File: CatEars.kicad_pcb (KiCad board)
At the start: 2 copper layers, 40.1 x 39 mm, 14 parts

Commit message: Added schematic and copper
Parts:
- removed Cuddle, Hugs, Meow, Nya, Puddle: WS2812B, LED_SMD:LED_WS2812B_PLCC4_5.0x5.0mm_P3.2mm
- removed In, Out: Conn_01x03_Female, Connector_PinSocket_2.54mm:PinSocket_1x03_P2.54mm_Vertical
- removed JP0: SolderJumper_2_Open, Jumper:SolderJumper-2_P1.3mm_Open_TrianglePad1.0x1.5mm
- removed R0: R, Capacitor_SMD:C_0805_2012Metric_Pad1.15x1.40mm_HandSolder
- added C5: C, Capacitor_SMD:C_0603_1608Metric_Pad1.05x0.95mm_HandSolder, F.Cu at (193.7, 131.4)
- added C6: C, Capacitor_SMD:C_0603_1608Metric_Pad1.05x0.95mm_HandSolder, B.Cu at (209.6, 128.9)
- added C7: C, Capacitor_SMD:C_0603_1608Metric_Pad1.05x0.95mm_HandSolder, B.Cu at (212.7, 134.0)
- added C8: C, Capacitor_SMD:C_0603_1608Metric_Pad1.05x0.95mm_HandSolder, F.Cu at (200.0, 128.9)
- added D0: WS2812B, LED_SMD:LED_WS2812B_PLCC4_5.0x5.0mm_P3.2mm, F.Cu at (215.9, 135.9)
- added D1: WS2812B, LED_SMD:LED_WS2812B_PLCC4_5.0x5.0mm_P3.2mm, F.Cu at (209.6, 120.0)
- added D2: WS2812B, LED_SMD:LED_WS2812B_PLCC4_5.0x5.0mm_P3.2mm, F.Cu at (200.0, 106.0)
- added D3: WS2812B, LED_SMD:LED_WS2812B_PLCC4_5.0x5.0mm_P3.2mm, F.Cu at (190.5, 120.0)
- added D4: WS2812B, LED_SMD:LED_WS2812B_PLCC4_5.0x5.0mm_P3.2mm, F.Cu at (184.2, 135.9)
- added D5: LED, LED_SMD:LED_0805_2012Metric_Pad1.15x1.40mm_HandSolder, F.Cu at (200.0, 111.8)
- added D6: LED, LED_SMD:LED_0805_2012Metric_Pad1.15x1.40mm_HandSolder, B.Cu at (198.1, 132.6)
- added D7: D_Schottky, Diode_SMD:D_SOT-23_ANK, B.Cu at (193.1, 133.9)
- added D8: D_Schottky, Diode_SMD:D_SOT-23_ANK, B.Cu at (213.7, 137.9)
- added H1: MountingHole_Pad, TestPoint:TestPoint_Pad_D1.5mm, B.Cu at (199.9, 104.1)
- added J1: Conn_01x02_Male, Connector_JST:JST_PH_B2B-PH-K_1x02_P2.00mm_Vertical, B.Cu at (207.3, 138.9)
- added J2: USB_B_Micro, Connector_USB:USB_Micro-B_GCT_USB3076-30-A, B.Cu at (190.9, 138.9)
- added J3: Conn_01x03, Connector_PinSocket_2.54mm:PinSocket_1x03_P2.54mm_Vertical, F.Cu at (197.5, 138.4)
- added J4: Conn_01x01, TestPoint:TestPoint_Pad_D1.0mm, B.Cu at (193.3, 130.8)
- added J5: Conn_01x01, TestPoint:TestPoint_Pad_D1.0mm, B.Cu at (191.5, 129.5)
- added J6: Conn_01x01, TestPoint:TestPoint_Pad_D1.0mm, B.Cu at (192.8, 121.2)
- added J7: Conn_01x01, TestPoint:TestPoint_Pad_D1.0mm, B.Cu at (192.0, 124.5)
- added JP1: SolderJumper_2_Open, Jumper:SolderJumper-2_P1.3mm_Open_TrianglePad1.0x1.5mm, F.Cu at (182.4, 140.3)
- added JP2: SolderJumper_2_Open, Jumper:SolderJumper-2_P1.3mm_Open_TrianglePad1.0x1.5mm, F.Cu at (217.6, 140.4)
- added R1: R, Resistor_SMD:R_0805_2012Metric_Pad1.15x1.40mm_HandSolder, B.Cu at (199.4, 117.1)
- added R2: R, Resistor_SMD:R_0805_2012Metric_Pad1.15x1.40mm_HandSolder, B.Cu at (202.4, 132.6)
- added R3: R, Resistor_SMD:R_0805_2012Metric_Pad1.15x1.40mm_HandSolder, F.Cu at (215.9, 129.8)
- added SW1: SW_Push, Button_Switch_SMD:SW_SPST_TL3342, F.Cu at (200.0, 132.7)
- added U1: ATSAMD21E18A-AU, Package_QFP:TQFP-32_7x7mm_P0.8mm, B.Cu at (200.0, 125.7)
- added U2: AP2112K-3.3, Package_TO_SOT_SMD:SOT-23-5, B.Cu at (208.5, 133.4)
- C0, C1, C2, C3, C4: moved to F.Cu
- moved C0 75.7 mm to (212.7, 130.8), turned to 90 degrees
- moved C1 64.5 mm to (207.0, 114.9), turned to 90 degrees
- moved C2 51.3 mm to (200.0, 109.9)
- moved C3 36.0 mm to (193.0, 114.9), turned to 90 degrees
- moved C4 27.5 mm to (186.7, 130.8), turned to 90 degrees
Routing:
- net GND: track 48.9 -> 145.8 mm, vias 3 -> 11
- net Net-(J3-Pad2): track 0.00 -> 36.3 mm
- net Net-(C7-Pad1): track 0.00 -> 34.5 mm, vias 0 -> 4
- net /USB_D-: track 0.00 -> 31.1 mm, vias 0 -> 4
- net /USB_D+: track 0.00 -> 29.2 mm, vias 0 -> 2
- net Net-(H1-Pad1): track 0.00 -> 28.9 mm, vias 0 -> 2
- net +3V3: track 110.0 -> 131.7 mm, vias 5 -> 4
- net Net-(R3-Pad1): track 0.00 -> 20.4 mm, vias 0 -> 3
- net Net-(J1-Pad2): track 17.8 -> 0.00 mm
- net Net-(J2-Pad6): track 0.00 -> 16.0 mm
- net Net-(C5-Pad2): track 0.00 -> 15.9 mm, vias 0 -> 1
- net Net-(SW1-Pad1): track 0.00 -> 11.7 mm, vias 0 -> 2
- net Net-(D0-Pad4): track 21.9 -> 13.4 mm, vias 1 -> 0
- net Net-(J4-Pad1): track 0.00 -> 6.10 mm
- net Net-(J5-Pad1): track 0.00 -> 5.89 mm
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- removed copper zone on B.Cu, net GND
- removed copper zone on F.Cu, net GND
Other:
- board size 40.1 x 39 mm -> 45.1 x 43.9 mm
- board text removed: "Input"
- board text removed: "Meow Meow Ears With <3 from Allie @GalaxyAllieCat"
- board text removed: "Output"

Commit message: Production Version with MCU - v2
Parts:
- :): renamed from J2; value USB_B_Micro -> USB_B_Micr
- turned 31 to 180 degrees
- renumbered J4 to 31, J5 to 32, J7 to 7, J6 to 8, D1 to A., J1 to Battery, D8 to Battery, R1 to Blink, SW1 to Boot, D4 to D., D2 to E., JP2 to In, D0 to M., D5 to Meow, D6 to On?, JP1 to Out, U2 to Pwr, D3 to R., R3 to Rin, D7 to USB
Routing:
- net GND: track 145.8 -> 153.5 mm, vias 11 -> 18
- added copper zone on B.Cu, net GND
- added copper zone on F.Cu, net GND
- added copper zone on B.Cu, net Net-(H1-Pad1)
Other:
- rule pad_to_mask_clearance: 0.051 -> 0.0508
- rule solder_mask_min_width: 0.25 -> 0.4
- board text added: "2020-01-12"
- board text added: "BIG"
- board text added: "Boop"
- board text added: "Dream"
- board text added: "Dreams"
- board text added: "If you believe it... You achieve it!"
- board text added: "Meow Meow Ears v2 With <3 from @GalaxyAllieCat"
- board text added: "NekoMimiLink"
- board text added: "Spot"

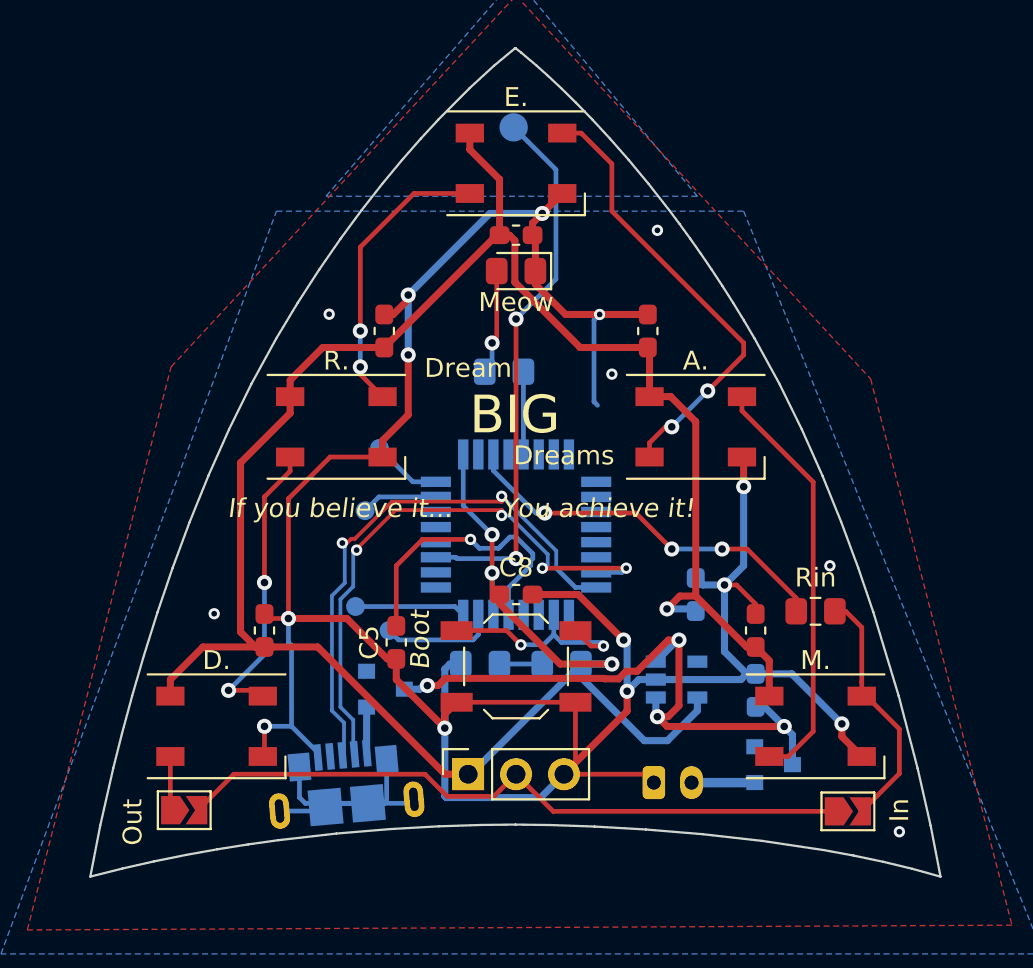
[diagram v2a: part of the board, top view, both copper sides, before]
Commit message: v2.1 - fix unconnected GND
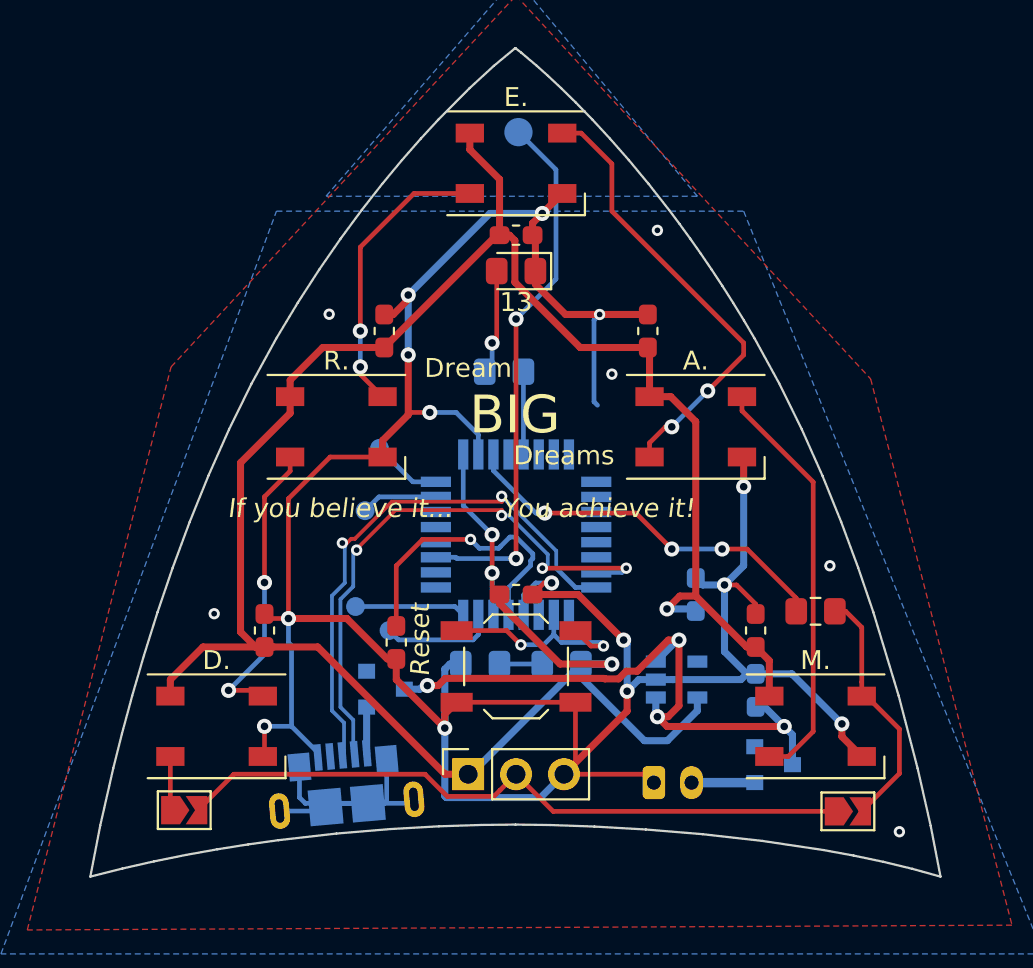
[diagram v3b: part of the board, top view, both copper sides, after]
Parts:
- J2: renamed from :); value USB_B_Micr -> USB_B_Micro
- moved H1 0.36 mm to (200.2, 104.4)
- gave numbers to parts that had none: 1
- renumbered Meow to 13, 32 to 31, 31 to 32, Battery to Batt, Battery to J1, Out to JP1, In to JP2, Blink to R1, Rin to R3, Boot to Reset, Pwr to U2
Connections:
- U1 pad 10: Net-(U1-Pad10) -> GND
- U1 pad 28: Net-(U1-Pad28) -> GND
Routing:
- net GND: track 153.5 -> 162.9 mm, vias 18 -> 20
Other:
- board text added: "Meow Meow Ears v2.1 With <3 from @GalaxyAllieCat"
- board text added: "Tickle"
- board text removed: "Boop"
- board text removed: "Meow Meow Ears v2 With <3 from @GalaxyAllieCat"

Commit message: v2.1 - Minor silkscreen edit
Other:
- board text added: "Free Hugs!"
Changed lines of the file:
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@@
   (general
     (thickness 1.6)
-    (drawings 95)
+    (drawings 96)
     (tracks 427)
     (zones 0)
@@
   (page A4)
   (layers
-    (0 F.Cu signal hide)
+    (0 F.Cu signal)
     (31 B.Cu signal)
     (32 B.Adhes user hide)
@@
     (42 Eco1.User user hide)
     (43 Eco2.User user hide)
-    (44 Edge.Cuts user hide)
+    (44 Edge.Cuts user)
     (45 Margin user hide)
-    (46 B.CrtYd user hide)
-    (47 F.CrtYd user hide)
+    (46 B.CrtYd user)
+    (47 F.CrtYd user)
     (48 B.Fab user hide)
     (49 F.Fab user hide)
@@
     (tags "capacitor handsolder")
     (attr smd)
-    (fp_text reference C7 (at 0 1.43 90) (layer B.SilkS)
+    (fp_text reference C7 (at 0 1.43 90) (layer B.SilkS) hide
       (effects (font (size 1 1) (thickness 0.15)) (justify mirror))
     )
@@
     (tags "capacitor handsolder")
     (attr smd)
-    (fp_text reference C6 (at -0.762 1.4605 270) (layer B.SilkS)
+    (fp_text reference C6 (at -0.762 1.4605 270) (layer B.SilkS) hide
       (effects (font (size 1 1) (thickness 0.15)) (justify mirror))
     )
@@
     )
   )
+  (gr_text "Free Hugs!" (at 213.995 128.143 90) (layer B.SilkS)
+    (effects (font (size 1 1) (thickness 0.15) italic) (justify mirror))
+  )
   (gr_text 2020-01-12 (at 186.4995 121.2215 65) (layer B.SilkS)
     (effects (font (size 1 1) (thickness 0.15)) (justify mirror))
@@
     (effects (font (size 1 1) (thickness 0.15) italic) (justify mirror))
   )
-  (gr_text Spot (at 194.945 106.553) (layer B.SilkS)
+  (gr_text Spot (at 195.961 106.553) (layer B.SilkS)
     (effects (font (size 1 1) (thickness 0.15)) (justify mirror))
   )
-  (gr_text Tickle (at 204.851 106.553) (layer B.SilkS)
+  (gr_text Tickle (at 203.708 106.553) (layer B.SilkS)
     (effects (font (size 1 1) (thickness 0.15)) (justify mirror))
   )

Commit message: v2.1 - Minor silkscreen edit
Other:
- board text added: "2020-01-20"
- board text removed: "2020-01-12"
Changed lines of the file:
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@@
     )
   )
-  (gr_text "Free Hugs!" (at 213.995 128.143 90) (layer B.SilkS)
-    (effects (font (size 1 1) (thickness 0.15) italic) (justify mirror))
+  (gr_text "Free Hugs!" (at 213.995 128.397 90) (layer B.SilkS)
+    (effects (font (size 1.2 1.2) (thickness 0.15) italic) (justify mirror))
   )
-  (gr_text 2020-01-12 (at 186.4995 121.2215 65) (layer B.SilkS)
+  (gr_text 2020-01-20 (at 186.4995 121.2215 65) (layer B.SilkS)
     (effects (font (size 1 1) (thickness 0.15)) (justify mirror))
   )
